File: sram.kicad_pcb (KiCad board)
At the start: 2 copper layers, 10 x 40 mm, 6 parts, among them J1 SRAM_pinheader_DIP32, U1 628128_TSOP32

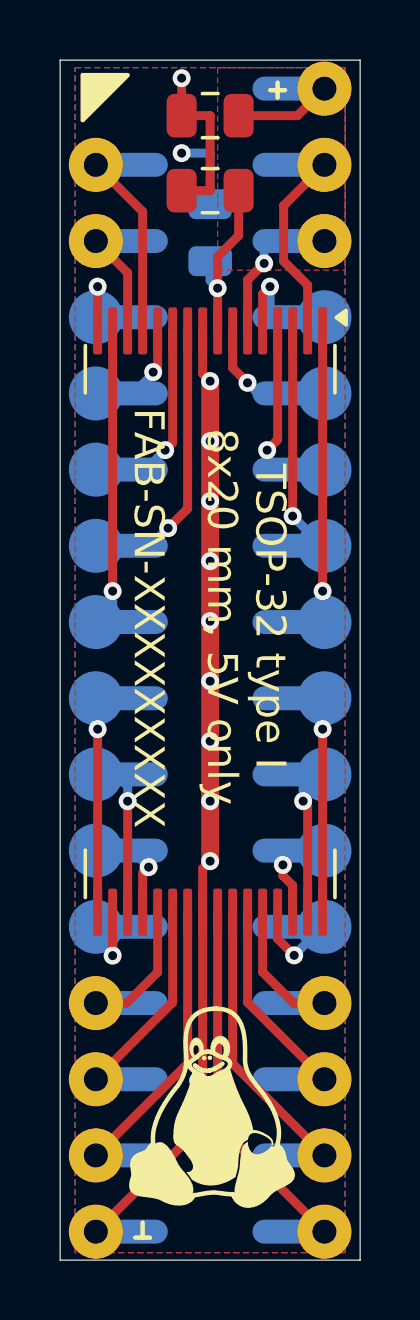
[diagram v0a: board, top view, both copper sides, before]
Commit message: Better labels for decoupling caps
Added DIP pinheader 3D model

Signed-off-by: Petr Cvek <petrcvekcz@gmail.com>
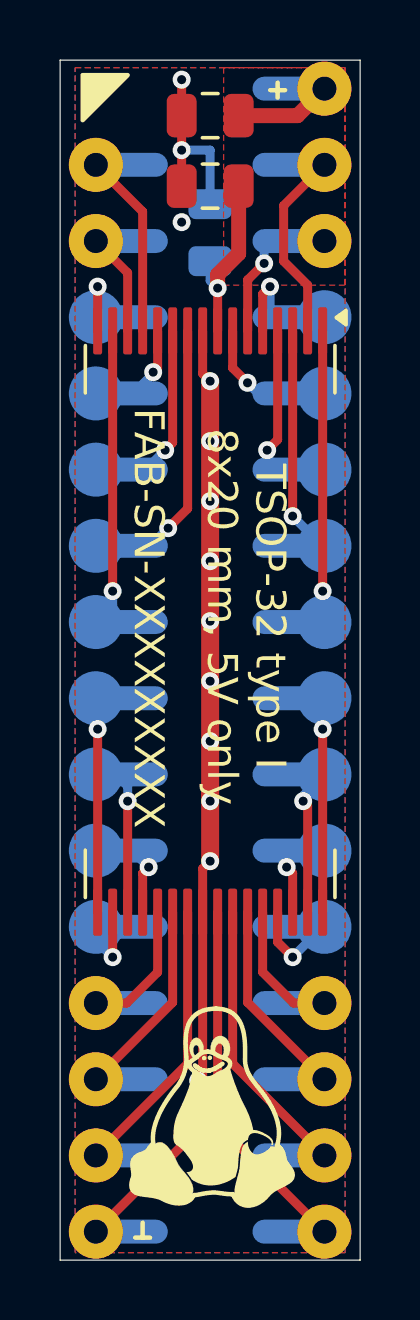
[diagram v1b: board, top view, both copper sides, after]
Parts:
- C1: value C_Polarized -> 100nF
- C2, C3: value C_Polarized -> 1uF
- moved C3 0.15 mm to (100.0, 59.2)
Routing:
- net GND: track 52.0 -> 50.7 mm, vias 12 -> 13
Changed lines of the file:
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@@
 			)
 		)
-		(property "Value" "C_Polarized"
+		(property "Value" "1uF"
 			(at 0 1.68 0)
 			(layer "F.Fab")
@@
 			)
 		)
-		(property "Datasheet" ""
+		(property "Datasheet" "~"
 			(at 0 0 180)
 			(unlocked yes)
@@
 		)
 		(property ki_fp_filters "CP_*")
-		(sheetname "Root")
+		(sheetname "/")
 		(sheetfile "sram.kicad_sch")
 		(attr smd)
@@
 		)
 		(property ki_fp_filters "*TSOP?I*11.8*8*P0.5mm* *TSOP?I*18.4*8*P0.5mm*")
-		(sheetname "Root")
+		(sheetname "/")
 		(sheetfile "sram.kicad_sch")
 		(attr smd)
@@
 	(footprint "Capacitor_SMD:C_0805_2012Metric"
 		(layer "F.Cu")
-		(at 100 59.35 180)
+		(at 100 59.2 180)
 		(descr "Capacitor SMD 0805 (2012 Metric), square (rectangular) end terminal, IPC_7351 nominal, (Body size source: IPC-SM-782 page 76, https://www.pcb-3d.com/wordpress/wp-content/uploads/ipc-sm-782a_amendment_1_and_2.pdf, https://docs.google.com/spreadsheets/d/1BsfQQcO9C6DZCsRaXUlFlo91Tg2WpOkGARC1WS5S8t0/edit?usp=sharing), generated with kicad-footprint-generator")
 		(tags "capacitor")
@@
 			)
 		)
-		(property "Value" "C_Polarized"
+		(property "Value" "1uF"
 			(at 0 1.68 0)
 			(layer "F.Fab")
@@
 			)
 		)
-		(property "Datasheet" ""
+		(property "Datasheet" "~"
 			(at 0 0 180)
 			(unlocked yes)
@@
 		)
 		(property ki_fp_filters "CP_*")
-		(sheetname "Root")
+		(sheetname "/")
 		(sheetfile "sram.kicad_sch")
 		(attr smd)
@@
 			)
 		)
-		(property "Value" "C_Polarized"
+		(property "Value" "100nF"
 			(at 0 -1.68 90)
 			(layer "B.Fab")
@@
 			)
 		)
-		(property "Datasheet" ""
+		(property "Datasheet" "~"
 			(at 0 0 270)
 			(unlocked yes)
@@
 			)
 		)
-		(property "Description" "Polarized capacitor"
+		(property "Description" "Unpolarized capacitor"
 			(at 0 0 270)
 			(unlocked yes)
@@
 			)
 		)
-		(property ki_fp_filters "CP_*")
-		(sheetname "Root")
+		(property ki_fp_filters "C_*")
+		(sheetname "/")
 		(sheetfile "sram.kicad_sch")
 		(attr smd)
@@
 		)
 		(property ki_fp_filters "DIP*W7.62mm*")
-		(sheetname "Root")
+		(sheetname "/")
 		(sheetfile "sram.kicad_sch")
 		(attr through_hole exclude_from_bom allow_missing_courtyard)
@@
 		)
 		(embedded_fonts no)
+		(model "${KIPRJMOD}/pcb_connector_370-80-116-00-001101.stp"
+			(offset
+				(xyz 0 3.85 6)
+			)
+			(scale
+				(xyz 1 1 1)
+			)
+			(rotate
+				(xyz 90 -0 -0)
+			)
+		)
+		(model "${KIPRJMOD}/pcb_connector_370-80-116-00-001101.stp"
+			(offset
+				(xyz 0 -3.8 6)
+			)
+			(scale
+				(xyz 1 1 1)
+			)
+			(rotate
+				(xyz 90 -0 -0)
+			)
+		)
 	)
 	(gr_poly
@@
 	)
 	(segment
-		(start 100.95 59.35)
-		(end 100.95 60.85)
-		(width 0.3)
+		(start 100.25 62.15)
+		(end 100.25 62.6)
+		(width 0.5)
 		(layer "F.Cu")
 		(net 1)
@@
 		(start 100.95 56.85)
 		(end 102.91 56.85)
-		(width 0.3)
+		(width 0.5)
 		(layer "F.Cu")
 		(net 1)
@@
 	)
 	(segment
-		(start 100.25 61.55)
-		(end 100.25 62.6)
-		(width 0.3)
+		(start 100.95 59.35)
+		(end 100.95 61.45)
+		(width 0.5)
 		(layer "F.Cu")
 		(net 1)
 	)
 	(segment
-		(start 100.95 60.85)
-		(end 100.25 61.55)
-		(width 0.3)
+		(start 102.91 56.85)
+		(end 103.81 55.95)
+		(width 0.5)
 		(layer "F.Cu")
 		(net 1)
 	)
 	(segment
-		(start 102.91 56.85)
-		(end 103.81 55.95)
-		(width 0.3)
+		(start 100.95 61.45)
+		(end 100.25 62.15)
+		(width 0.5)
 		(layer "F.Cu")
 		(net 1)
@@
 	)
 	(segment
-		(start 99.3 59.35)
-		(end 100 59.35)
-		(width 0.3)
-		(layer "F.Cu")
-		(net 2)
-	)
-	(segment
 		(start 99.75 81.95)
 		(end 99.75 90.49)
@@
 	)
 	(segment
-		(start 100 71.5)
-		(end 100 79.5)
+		(start 99.05 59.35)
+		(end 99.05 56.85)
 		(width 0.3)
 		(layer "F.Cu")
@@
 	)
 	(segment
-		(start 100 65.7)
-		(end 99.75 65.45)
+		(start 100 71.5)
+		(end 100 79.5)
 		(width 0.3)
 		(layer "F.Cu")
@@
 	)
 	(segment
-		(start 99.05 56.85)
-		(end 99.05 55.6)
+		(start 100 65.7)
+		(end 99.75 65.45)
 		(width 0.3)
 		(layer "F.Cu")
@@
 	)
 	(segment
-		(start 100 56.85)
-		(end 99.05 56.85)
-		(width 0.3)
+		(start 100 65.7)
+		(end 100 79.5)
+		(width 0.6)
 		(layer "F.Cu")
 		(net 2)
 	)
 	(segment
-		(start 100 65.7)
-		(end 100 79.5)
-		(width 0.6)
+		(start 99.3 59.35)
+		(end 99.05 59.35)
+		(width 0.3)
 		(layer "F.Cu")
 		(net 2)
@@
 	)
 	(segment
-		(start 100 59.35)
-		(end 100 56.85)
+		(start 99.05 55.65)
+		(end 99.05 56.85)
 		(width 0.3)
 		(layer "F.Cu")
@@
 	)
 	(via
-		(at 99.05 55.6)
+		(at 99.05 60.4)
+		(size 0.6)
+		(drill 0.3)
+		(layers "F.Cu" "B.Cu")
+		(free yes)
+		(net 2)
+	)
+	(via
+		(at 99.05 55.65)
 		(size 0.6)
 		(drill 0.3)
@@
 	)
 	(via
-		(at 99.05 58.1)
+		(at 99.05 58)
 		(size 0.6)
 		(drill 0.3)
@@
 	)
 	(segment
-		(start 100 58.1)
-		(end 99.05 58.1)
+		(start 99.05 58)
+		(end 100 58)
 		(width 0.3)
 		(layer "B.Cu")
@@
 	)
 	(segment
-		(start 100 59.8)
-		(end 100 58.1)
+		(start 100 58)
+		(end 100 59.8)
 		(width 0.3)
 		(layer "B.Cu")
@@
 	)
 	(segment
-		(start 102.425 81.825)
-		(end 102.425 82.18438)
+		(start 102.75 82.1)
+		(end 102.75 83.4)
 		(width 0.3)
 		(layer "F.Cu")
@@
 	)
 	(segment
-		(start 102.425 82.18438)
-		(end 102.75 82.50938)
-		(width 0.3)
-		(layer "F.Cu")
-		(net 9)
-	)
-	(segment
-		(start 102.75 82.50938)
-		(end 102.75 83.4)
+		(start 102.55 81.9)
+		(end 102.75 82.1)
 		(width 0.3)
 		(layer "F.Cu")
@@
 	)
 	(via
-		(at 102.425 81.825)
+		(at 102.55 81.9)
 		(size 0.6)
 		(drill 0.3)
@@
 	)
 	(segment
+		(start 102.6 81.65)
+		(end 102.9 81.35)
+		(width 0.3)
+		(layer "B.Cu")
+		(net 9)
+	)
+	(segment
+		(start 102.55 81.9)
+		(end 102.6 81.85)
+		(width 0.3)
+		(layer "B.Cu")
+		(net 9)
+	)
+	(segment
 		(start 102.9 81.35)
 		(end 103.81 81.35)
@@
 	)
 	(segment
-		(start 102.425 81.825)
-		(end 102.9 81.35)
+		(start 102.6 81.85)
+		(end 102.6 81.65)
 		(width 0.3)
 		(layer "B.Cu")
@@
 	)
 	(segment
-		(start 103.1 79.2)
+		(start 103.81 78.81)
 		(end 103.49 78.81)
 		(width 0.3)
@@
 	)
 	(segment
+		(start 103.1 79.52)
+		(end 103.81 78.81)
+		(width 0.3)
+		(layer "B.Cu")
+		(net 19)
+	)
+	(segment
 		(start 103.1 79.7)
-		(end 103.1 79.2)
+		(end 103.1 79.52)
 		(width 0.3)
 		(layer "B.Cu")
@@
 	(segment
 		(start 96.75 83.4)
-		(end 96.75 84.85)
+		(end 96.75 84.9)
 		(width 0.3)
 		(layer "F.Cu")
@@
 	)
 	(via
-		(at 96.75 84.85)
+		(at 96.75 84.9)
 		(size 0.6)
 		(drill 0.3)
@@
 	)
 	(segment
-		(start 96.75 84.45)
-		(end 96.19 83.89)
+		(start 96.75 84.9)
+		(end 96.2 84.35)
 		(width 0.3)
 		(layer "B.Cu")
@@
 	)
 	(segment
-		(start 96.75 84.85)
-		(end 96.75 84.45)
+		(start 96.2 84.35)
+		(end 96.2 83.9)
 		(width 0.3)
 		(layer "B.Cu")
@@
 	)
 	(segment
-		(start 102.8 84.84062)
-		(end 102.25 84.29062)
+		(start 96.2 83.9)
+		(end 96.19 83.89)
+		(width 0.3)
+		(layer "B.Cu")
+		(net 24)
+	)
+	(segment
+		(start 102.25 84.4)
+		(end 102.25 83.4)
 		(width 0.3)
 		(layer "F.Cu")
@@
 	)
 	(segment
-		(start 102.25 84.29062)
-		(end 102.25 83.4)
+		(start 102.75 84.9)
+		(end 102.25 84.4)
 		(width 0.3)
 		(layer "F.Cu")
@@
 	)
 	(via
-		(at 102.8 84.84062)
+		(at 102.75 84.9)
 		(size 0.6)
 		(drill 0.3)
@@
 	)
 	(segment
-		(start 102.8 84.84062)
+		(start 103.75062 83.89938)
 		(end 103.75062 83.89)
 		(width 0.3)
@@
 	)
 	(segment
+		(start 102.75 84.9)
+		(end 103.75062 83.89938)
+		(width 0.3)
+		(layer "B.Cu")
+		(net 25)
+	)
+	(segment
 		(start 101.245 65.755)
 		(end 100.75 65.26)
@@
 		(polygon
 			(pts
-				(xy 104.5 55.25) (xy 100.25 55.25) (xy 100.25 62) (xy 104.5 62)
+				(xy 104.5 55.25) (xy 100.45 55.25) (xy 100.45 62.5) (xy 104.5 62.5)
 			)
 		)
